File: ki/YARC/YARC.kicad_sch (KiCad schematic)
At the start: 0 parts

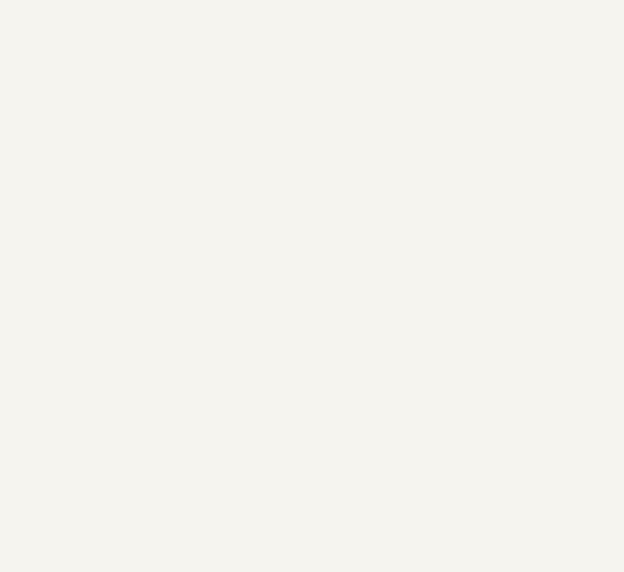
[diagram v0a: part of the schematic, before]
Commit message: Add microcode engine to KiCad. Minor updates to README.
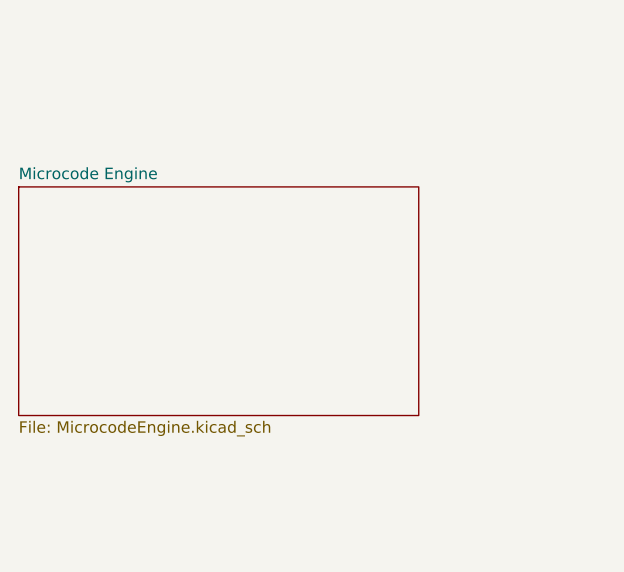
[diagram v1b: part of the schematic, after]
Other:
- added sheet Microcode Engine (MicrocodeEngine.kicad_sch)
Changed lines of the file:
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@@
+    )
+  )
+  (sheet (at 29.21 172.72) (size 44.45 25.4) (fields_autoplaced)
+    (stroke (width 0.1524) (type solid) (color 0 0 0 0))
+    (fill (color 0 0 0 0.0000))
+    (property "Sheet name" "Microcode Engine" (id 0) (at 29.21 172.0084 0)
+      (effects (font (size 1.27 1.27)) (justify left bottom))
+    )
+    (property "Sheet file" "MicrocodeEngine.kicad_sch" (id 1) (at 29.21 198.7046 0)
+      (effects (font (size 1.27 1.27)) (justify left top))
     )
   )
@@
     (path "/4512e1de-1ae8-4271-aab5-cfad75ab4cbf" (page "3"))
     (path "/32a6a89d-8e27-4c41-a8a1-866f443f001b" (page "4"))
+    (path "/898bc8c4-26bf-49d8-bb4c-382409bb277a" (page "5"))
   )
   (symbol_instances
@@
       (reference "U30") (unit 1) (value "74HC245") (footprint "")
     )
+    (path "/898bc8c4-26bf-49d8-bb4c-382409bb277a/0184d394-883e-43ae-8d34-94bab0ae7228"
+      (reference "U?") (unit 1) (value "74LS574") (footprint "")
+    )
+    (path "/898bc8c4-26bf-49d8-bb4c-382409bb277a/1c8135b7-f279-409a-af45-66e5c2a7f1c7"
+      (reference "U?") (unit 1) (value "AS6C6264") (footprint "")
+    )
+    (path "/898bc8c4-26bf-49d8-bb4c-382409bb277a/4115d916-02e2-4a18-82cb-a96835d547d0"
+      (reference "U?") (unit 1) (value "74HC245") (footprint "")
+    )
+    (path "/898bc8c4-26bf-49d8-bb4c-382409bb277a/412bb8a2-b81f-4e41-8749-1ac5a36dfc26"
+      (reference "U?") (unit 1) (value "74LS574") (footprint "")
+    )
+    (path "/898bc8c4-26bf-49d8-bb4c-382409bb277a/7edec757-24b8-481f-a696-582c714a74a1"
+      (reference "U?") (unit 1) (value "AS6C6264") (footprint "")
+    )
+    (path "/898bc8c4-26bf-49d8-bb4c-382409bb277a/84bb7c32-34c3-4d85-9b06-8754ebd07667"
+      (reference "U?") (unit 1) (value "74LS574") (footprint "")
+    )
+    (path "/898bc8c4-26bf-49d8-bb4c-382409bb277a/9deb303f-f753-4af2-b446-d25f75f59380"
+      (reference "U?") (unit 1) (value "74LS574") (footprint "")
+    )
+    (path "/898bc8c4-26bf-49d8-bb4c-382409bb277a/9e561e29-8fae-457a-9111-42073e978b8f"
+      (reference "U?") (unit 1) (value "AS6C6264") (footprint "")
+    )
+    (path "/898bc8c4-26bf-49d8-bb4c-382409bb277a/a27df806-f11e-47cf-b440-2b742932b664"
+      (reference "U?") (unit 1) (value "74HC245") (footprint "")
+    )
+    (path "/898bc8c4-26bf-49d8-bb4c-382409bb277a/a533ba79-7f6b-40a9-aa41-fc8bce60aa08"
+      (reference "U?") (unit 1) (value "74HC245") (footprint "")
+    )
+    (path "/898bc8c4-26bf-49d8-bb4c-382409bb277a/e3989918-0725-47f7-b9e1-48b570b0e233"
+      (reference "U?") (unit 1) (value "AS6C6264") (footprint "")
+    )
+    (path "/898bc8c4-26bf-49d8-bb4c-382409bb277a/edcd72f5-8b8e-4cf4-82f5-4dd3550e28b5"
+      (reference "U?") (unit 1) (value "74HC245") (footprint "")
+    )
     (path "/4512e1de-1ae8-4271-aab5-cfad75ab4cbf/f8ebbe10-0751-4bba-bb4f-21bf35b8e2ef"

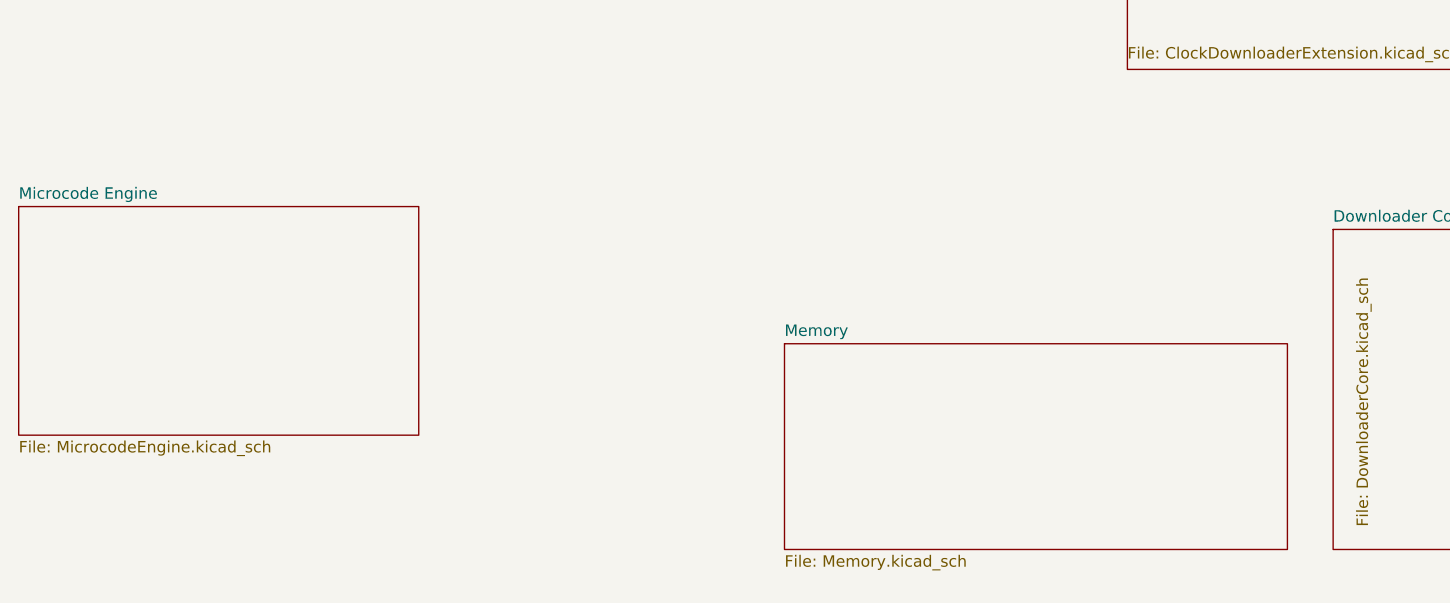
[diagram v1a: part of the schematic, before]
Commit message: Update README and docs. Progress on KiCad ucode schematic. Moved yasm code.
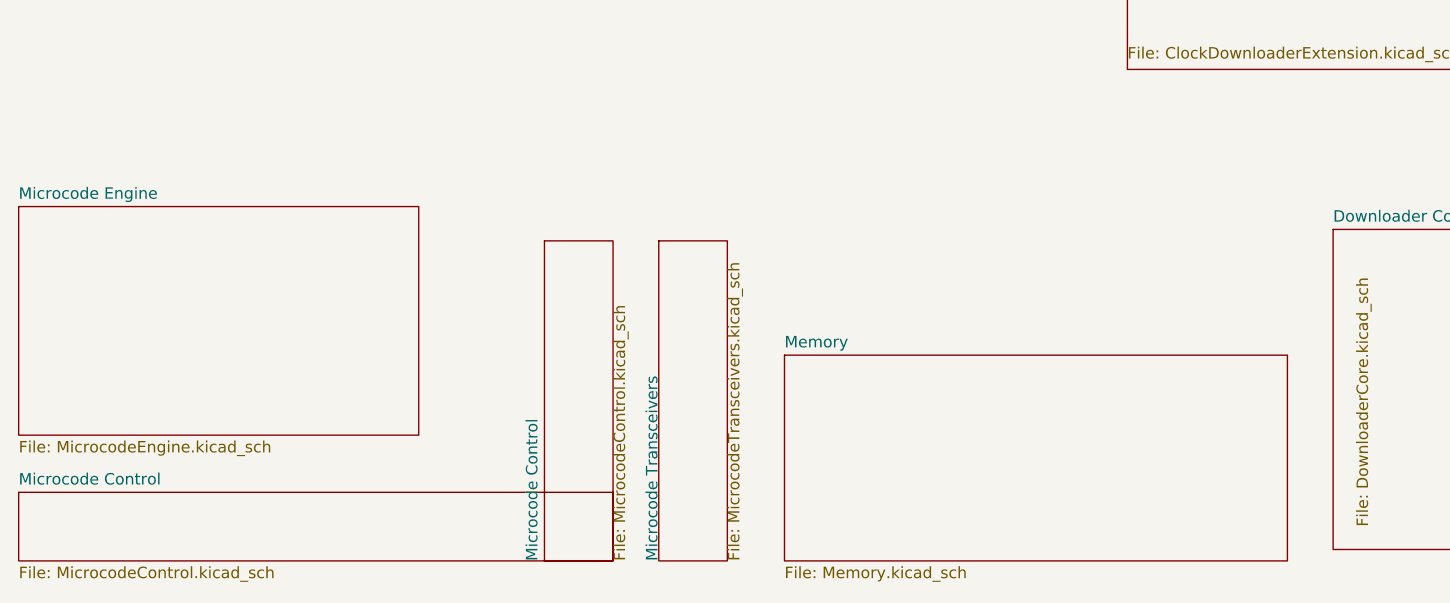
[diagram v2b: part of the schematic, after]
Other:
- added sheet Microcode Control (MicrocodeControl.kicad_sch)
- added sheet Microcode Transceivers (MicrocodeTransceivers.kicad_sch)
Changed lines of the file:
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@@
     )
   )
-  (sheet (at 114.3 187.96) (size 55.88 22.86) (fields_autoplaced)
-    (stroke (width 0.1524) (type solid) (color 0 0 0 0))
-    (fill (color 0 0 0 0.0000))
-    (property "Sheet name" "Memory" (id 0) (at 114.3 187.2484 0)
-      (effects (font (size 1.27 1.27)) (justify left bottom))
-    )
-    (property "Sheet file" "Memory.kicad_sch" (id 1) (at 114.3 211.4046 0)
+  (sheet (at 114.3 189.23) (size 55.88 22.86) (fields_autoplaced)
+    (stroke (width 0.1524) (type solid) (color 0 0 0 0))
+    (fill (color 0 0 0 0.0000))
+    (property "Sheet name" "Memory" (id 0) (at 114.3 188.5184 0)
+      (effects (font (size 1.27 1.27)) (justify left bottom))
+    )
+    (property "Sheet file" "Memory.kicad_sch" (id 1) (at 114.3 212.6746 0)
+      (effects (font (size 1.27 1.27)) (justify left top))
+    )
+  )
+  (sheet (at 29.21 204.47) (size 66.04 7.62) (fields_autoplaced)
+    (stroke (width 0.1524) (type solid) (color 0 0 0 0))
+    (fill (color 0 0 0 0.0000))
+    (property "Sheet name" "Microcode Control" (id 0) (at 29.21 203.7584 0)
+      (effects (font (size 1.27 1.27)) (justify left bottom))
+    )
+    (property "Sheet file" "MicrocodeControl.kicad_sch" (id 1) (at 29.21 212.6746 0)
       (effects (font (size 1.27 1.27)) (justify left top))
     )
@@
     )
   )
+  (sheet (at 100.33 176.53) (size 7.62 35.56)
+    (stroke (width 0.1524) (type solid) (color 0 0 0 0))
+    (fill (color 0 0 0 0.0000))
+    (property "Sheet name" "Microcode Transceivers" (id 0) (at 100.33 212.09 90)
+      (effects (font (size 1.27 1.27)) (justify left bottom))
+    )
+    (property "Sheet file" "MicrocodeTransceivers.kicad_sch" (id 1) (at 107.95 212.09 90)
+      (effects (font (size 1.27 1.27)) (justify left top))
+    )
+  )
   (sheet (at 29.21 172.72) (size 44.45 25.4) (fields_autoplaced)
     (stroke (width 0.1524) (type solid) (color 0 0 0 0))
@@
     )
     (property "Sheet file" "MicrocodeEngine.kicad_sch" (id 1) (at 29.21 198.7046 0)
+      (effects (font (size 1.27 1.27)) (justify left top))
+    )
+  )
+  (sheet (at 87.63 176.53) (size 7.62 35.56)
+    (stroke (width 0.1524) (type solid) (color 0 0 0 0))
+    (fill (color 0 0 0 0.0000))
+    (property "Sheet name" "Microcode Control" (id 0) (at 86.995 212.09 90)
+      (effects (font (size 1.27 1.27)) (justify left bottom))
+    )
+    (property "Sheet file" "MicrocodeControl.kicad_sch" (id 1) (at 95.25 212.09 90)
       (effects (font (size 1.27 1.27)) (justify left top))
     )
@@
     (path "/32a6a89d-8e27-4c41-a8a1-866f443f001b" (page "4"))
     (path "/898bc8c4-26bf-49d8-bb4c-382409bb277a" (page "5"))
+    (path "/39927ce2-e2db-424f-b8d0-f15d67a3ef8b" (page "6"))
+    (path "/a3892bed-2422-46c3-a2f7-c55c7ea6ac93" (page "7"))
+    (path "/5c3a56e1-a539-47ae-9041-458228256291" (page "8"))
   )
   (symbol_instances
@@
       (reference "#PWR0119") (unit 1) (value "GND") (footprint "")
     )
+    (path "/898bc8c4-26bf-49d8-bb4c-382409bb277a/d09a736e-a237-4ede-b1bb-2b5040ba1f90"
+      (reference "#PWR?") (unit 1) (value "VCC") (footprint "")
+    )
     (path "/baeeec1c-6d89-4b09-ba07-b183ebc66f47/ab26a42e-b7f6-4a80-b26c-c01085e448c7"

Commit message: Much work on ALU and registers
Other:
- added sheet FlagLogic (FlagLogic.kicad_sch)
- added sheet GeneralRegisters (GeneralRegisters.kicad_sch)
- added sheet Stacks (Stacks.kicad_sch)

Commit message: Adding microcode control lines from Nano
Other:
- added sheet South Central (SouthCentral.kicad_sch)
